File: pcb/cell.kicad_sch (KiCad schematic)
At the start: 29 parts, among them U1 MC74HC151ADTR2G, U2 SN74LVC1G74

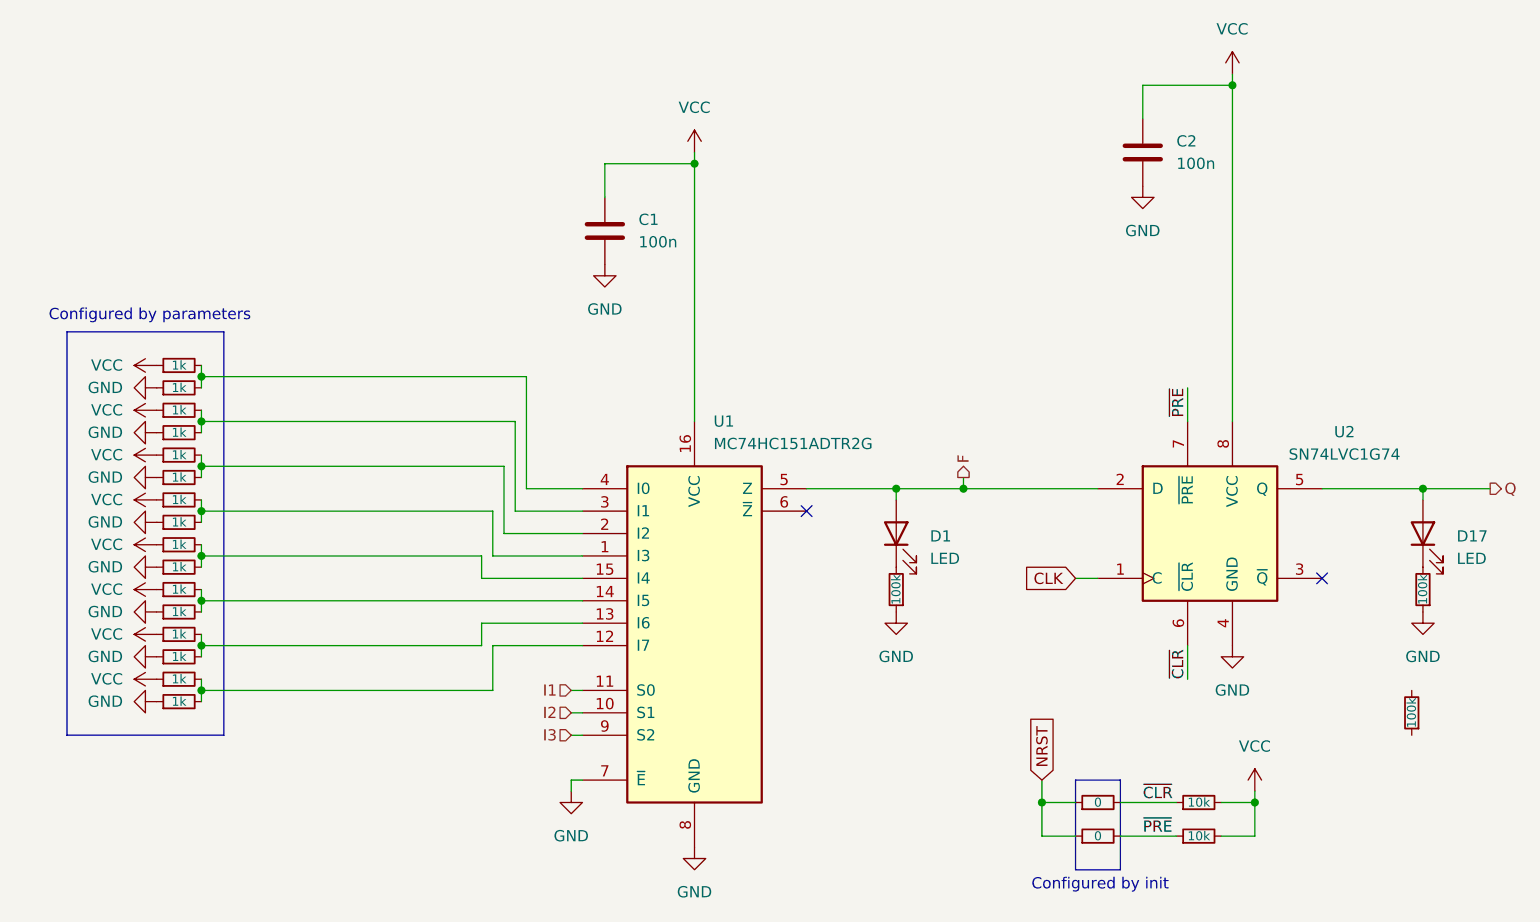
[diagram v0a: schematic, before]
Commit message: Add output LED array
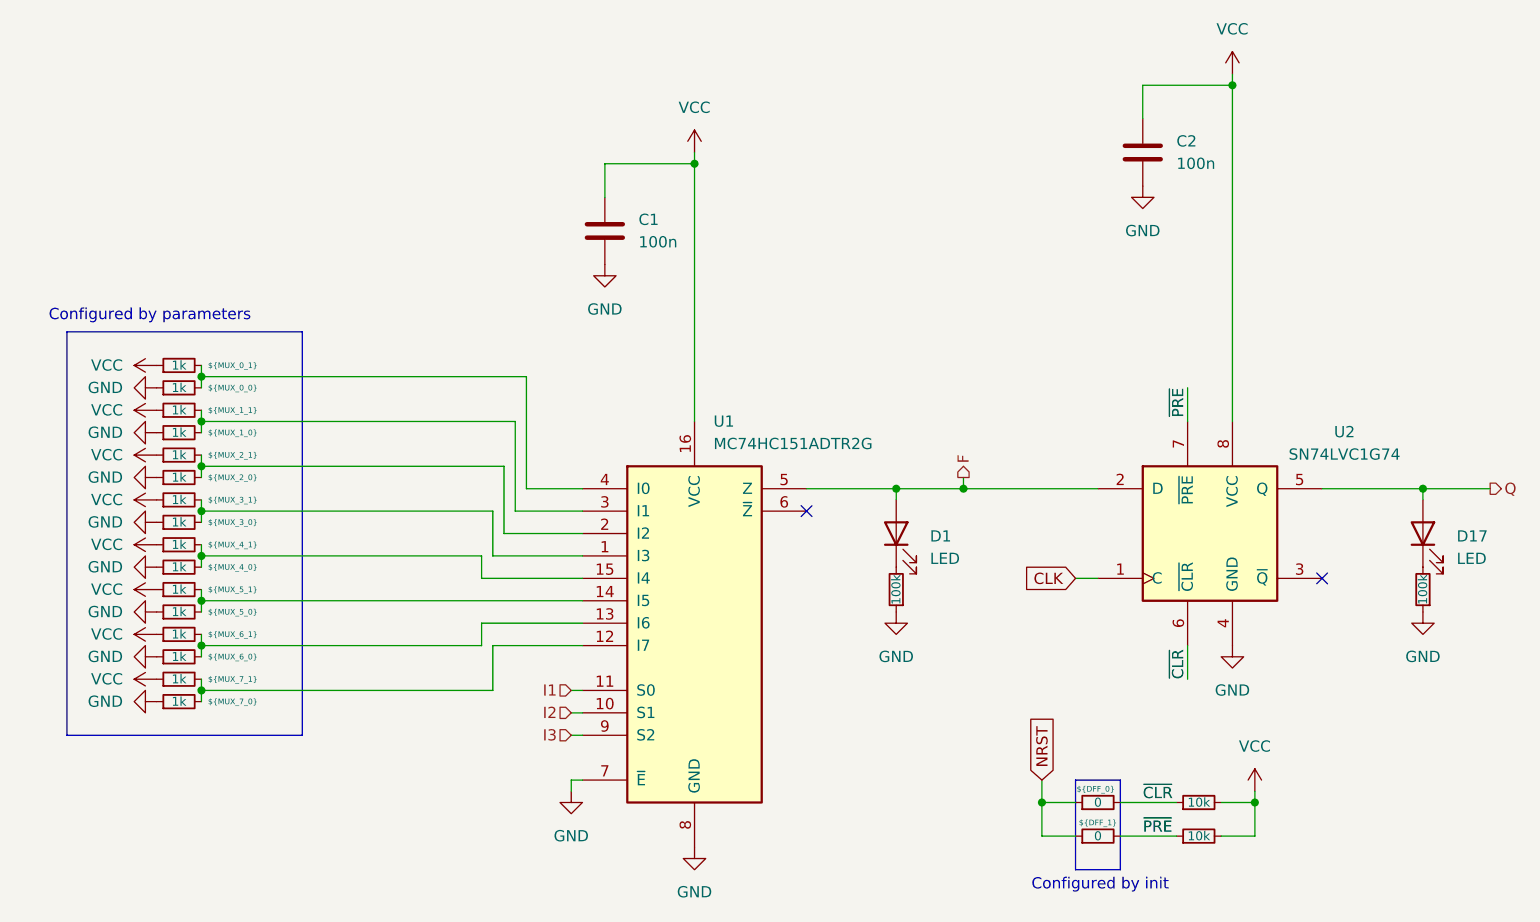
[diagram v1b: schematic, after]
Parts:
- removed R40: 100k, Resistor_SMD:R_0402_1005Metric, symbol Device:R_Small
- R1: POPULATE (none) -> ${MUX_0_0}
- R10: POPULATE (none) -> ${MUX_4_0}
- R11: POPULATE (none) -> ${MUX_5_1}
- R12: POPULATE (none) -> ${MUX_5_0}
- R13: POPULATE (none) -> ${MUX_6_1}
- R14: POPULATE (none) -> ${MUX_6_0}
- R15: POPULATE (none) -> ${MUX_7_1}
- R16: POPULATE (none) -> ${MUX_7_0}
- R2: POPULATE (none) -> ${MUX_1_1}
- R3: POPULATE (none) -> ${MUX_0_1}
- R35: POPULATE (none) -> ${DFF_0}
- R36: POPULATE (none) -> ${DFF_1}
- R4: POPULATE (none) -> ${MUX_1_0}
- R5: POPULATE (none) -> ${MUX_2_1}
- R6: ${MUX_2_0} (none) -> ${MUX_2_0}
- R7: POPULATE (none) -> ${MUX_3_1}
- R8: POPULATE (none) -> ${MUX_3_0}
- R9: POPULATE (none) -> ${MUX_4_1}
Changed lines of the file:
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@@
 	(rectangle
 		(start 68.58 58.42)
-		(end 86.36 104.14)
+		(end 95.25 104.14)
 		(stroke
 			(width 0)
@@
 			)
 		)
+		(property "POPULATE" "${MUX_0_1}"
+			(at 87.376 62.23 90)
+			(effects
+				(font
+					(size 0.635 0.635)
+				)
+			)
+		)
 		(pin "2"
 		)
@@
 			)
 		)
+		(property "POPULATE" "${MUX_4_0}"
+			(at 87.376 85.09 90)
+			(effects
+				(font
+					(size 0.635 0.635)
+				)
+			)
+		)
 		(pin "2"
 		)
@@
 			)
 		)
+		(property "POPULATE" "${MUX_5_1}"
+			(at 87.376 87.63 90)
+			(effects
+				(font
+					(size 0.635 0.635)
+				)
+			)
+		)
 		(pin "2"
 		)
@@
 			)
 		)
+		(property "POPULATE" "${MUX_2_1}"
+			(at 87.376 72.39 90)
+			(effects
+				(font
+					(size 0.635 0.635)
+				)
+			)
+		)
 		(pin "2"
 		)
@@
 			)
 		)
+		(property "POPULATE" "${DFF_1}"
+			(at 185.42 114.046 90)
+			(effects
+				(font
+					(size 0.635 0.635)
+				)
+			)
+		)
 		(pin "2"
 		)
@@
 			)
 		)
+		(property "POPULATE" "${MUX_1_0}"
+			(at 87.376 69.85 90)
+			(effects
+				(font
+					(size 0.635 0.635)
+				)
+			)
+		)
 		(pin "2"
 		)
@@
 			)
 		)
+		(property "POPULATE" "${DFF_0}"
+			(at 185.166 110.236 90)
+			(effects
+				(font
+					(size 0.635 0.635)
+				)
+			)
+		)
 		(pin "2"
 		)
@@
 			)
 		)
+		(property "POPULATE" "${MUX_7_1}"
+			(at 87.376 97.79 90)
+			(effects
+				(font
+					(size 0.635 0.635)
+				)
+			)
+		)
 		(pin "2"
 		)
@@
 			)
 		)
+		(property "POPULATE" "${MUX_4_1}"
+			(at 87.376 82.55 90)
+			(effects
+				(font
+					(size 0.635 0.635)
+				)
+			)
+		)
 		(pin "2"
 		)
@@
 			)
 		)
+		(property "POPULATE" "${MUX_3_1}"
+			(at 87.376 77.47 90)
+			(effects
+				(font
+					(size 0.635 0.635)
+				)
+			)
+		)
 		(pin "2"
 		)
@@
 			)
 		)
+		(property "POPULATE" "${MUX_3_0}"
+			(at 87.376 80.01 90)
+			(effects
+				(font
+					(size 0.635 0.635)
+				)
+			)
+		)
 		(pin "2"
 		)
@@
 			)
 		)
+		(property "POPULATE" "${MUX_1_1}"
+			(at 87.376 67.31 90)
+			(effects
+				(font
+					(size 0.635 0.635)
+				)
+			)
+		)
 		(pin "2"
 		)
@@
 			)
 		)
+		(property "POPULATE" "${MUX_0_0}"
+			(at 87.376 64.77 90)
+			(effects
+				(font
+					(size 0.635 0.635)
+				)
+			)
+		)
 		(pin "2"
 		)
@@
 			)
 		)
+		(property "POPULATE" "${MUX_6_1}"
+			(at 87.376 92.71 90)
+			(effects
+				(font
+					(size 0.635 0.635)
+				)
+			)
+		)
 		(pin "2"
 		)
@@
 			)
 		)
+		(property "${MUX_2_0}" "${MUX_2_0}"
+			(at 87.376 74.93 90)
+			(effects
+				(font
+					(size 0.635 0.635)
+				)
+			)
+		)
 		(pin "2"
 		)
@@
 			)
 		)
+		(property "POPULATE" "${MUX_7_0}"
+			(at 87.376 100.33 90)
+			(effects
+				(font
+					(size 0.635 0.635)
+				)
+			)
+		)
 		(pin "2"
 		)
@@
 			)
 		)
-		(pin "2"
-		)
-		(pin "1"
-		)
-		(instances
-			(project "74aoc"
-				(path "/976aec4d-1ebe-44c6-a45c-c82e0c896ea2/7fc5f80c-ae61-41ba-be16-2c640c59fc3f"
-					(reference "R12")
-					(unit 1)
-				)
-			)
-		)
-	)
-	(symbol
-		(lib_id "Device:R_Small")
-		(at 220.98 101.6 180)
-		(unit 1)
-		(exclude_from_sim no)
-		(in_bom yes)
-		(on_board yes)
-		(dnp no)
-		(property "Reference" "R40"
-			(at 222.25 98.806 90)
+		(property "POPULATE" "${MUX_5_0}"
+			(at 87.376 90.17 90)
 			(effects
 				(font
-					(size 1.016 1.016)
+					(size 0.635 0.635)
 				)
-				(hide yes)
-			)
-		)
-		(property "Value" "100k"
-			(at 220.98 101.6 90)
-			(effects
-				(font
-					(size 1.016 1.016)
-				)
-			)
-		)
-		(property "Footprint" "Resistor_SMD:R_0402_1005Metric"
-			(at 220.98 101.6 0)
-			(effects
-				(font
-					(size 1.27 1.27)
-				)
-				(hide yes)
-			)
-		)
-		(property "Datasheet" "~"
-			(at 220.98 101.6 0)
-			(effects
-				(font
-					(size 1.27 1.27)
-				)
-				(hide yes)
-			)
-		)
-		(property "Description" "Resistor, small symbol"
-			(at 220.98 101.6 0)
-			(effects
-				(font
-					(size 1.27 1.27)
-				)
-				(hide yes)
 			)
 		)
@@
 			(project "74aoc"
 				(path "/976aec4d-1ebe-44c6-a45c-c82e0c896ea2/7fc5f80c-ae61-41ba-be16-2c640c59fc3f"
-					(reference "R40")
+					(reference "R12")
 					(unit 1)
 				)
@@
 			)
 		)
+		(property "POPULATE" "${MUX_6_0}"
+			(at 87.376 95.25 90)
+			(effects
+				(font
+					(size 0.635 0.635)
+				)
+			)
+		)

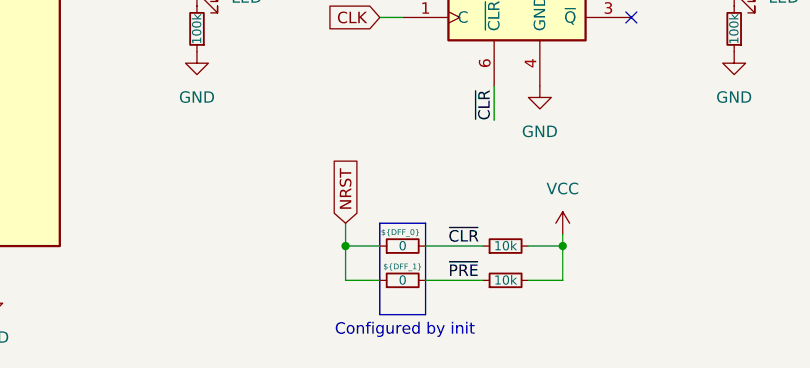
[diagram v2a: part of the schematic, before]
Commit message: Initialize all DFFs to 0
Oops did not realize that nextpnr can only do 1 anyway...
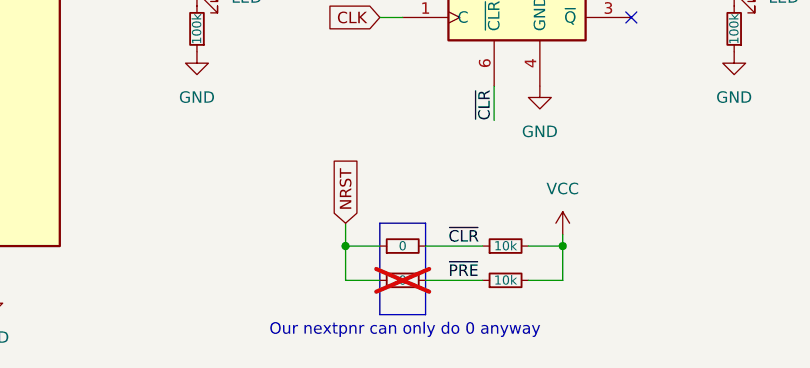
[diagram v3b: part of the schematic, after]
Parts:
- R35: POPULATE ${DFF_0} -> (none)
- R36: POPULATE ${DFF_1} -> (none); now not fitted
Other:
- note added: "Our nextpnr can only do 0 anyway"
- note removed: "Configured by init"
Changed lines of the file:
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@@
 		)
 	)
-	(text "Configured by init"
+	(text "Our nextpnr can only do 0 anyway"
 		(exclude_from_sim no)
 		(at 185.674 121.158 0)
@@
 		(in_bom yes)
 		(on_board yes)
-		(dnp no)
+		(dnp yes)
 		(property "Reference" "R36"
 			(at 188.214 116.84 90)
@@
 			)
 		)
-		(property "POPULATE" "${DFF_1}"
-			(at 185.42 114.046 90)
-			(effects
-				(font
-					(size 0.635 0.635)
-				)
-			)
-		)
 		(pin "2"
 		)
@@
 			)
 		)
-		(property "POPULATE" "${DFF_0}"
-			(at 185.166 110.236 90)
-			(effects
-				(font
-					(size 0.635 0.635)
-				)
-			)
-		)

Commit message: PCB prettification
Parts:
- U2: POPULATE (none) -> ${USE_DFF}
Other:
- note added: "Nextpnr can only do 0 anyway"
- note removed: "Our nextpnr can only do 0 anyway"
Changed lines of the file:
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@@
 		)
 	)
-	(text "Our nextpnr can only do 0 anyway"
+	(text "Nextpnr can only do 0 anyway"
 		(exclude_from_sim no)
 		(at 185.674 121.158 0)
@@
 			(at 198.12 81.28 0)
 			(effects
+				(font
+					(size 1.27 1.27)
+				)
+				(hide yes)
+			)
+		)
+		(property "POPULATE" "${USE_DFF}"
+			(at 198.12 81.28 0)
+			(effects

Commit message: Tag unused Muxes/DFFs for not-populating
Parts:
- U1: POPULATE (none) -> ${USE_MUX}
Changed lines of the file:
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@@
+			)
+		)
+		(property "POPULATE" "${USE_MUX}"
+			(at 139.7 91.44 0)
+			(effects
+				(font
+					(size 1.27 1.27)
+				)
+				(hide yes)
 			)
 		)

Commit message: Add LCSC codes to everything that did not have them yet
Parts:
- C1, C2: LCSC (none) -> C1525
- R1, R10, R11, R12, R13, R14, R15, R16, R2, R3, R4, R5, R6, R7, R8, R9: LCSC (none) -> C11702
- R17, R34: LCSC (none) -> C25744
- R35, R36: LCSC (none) -> C17168
- R37, R38: LCSC (none) -> C25741
- U1: LCSC (none) -> C152523
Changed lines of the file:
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@@
 			)
 		)
+		(property "LCSC" "C11702"
+			(at 81.28 62.23 90)
+			(effects
+				(font
+					(size 1.27 1.27)
+				)
+				(hide yes)
+			)
+		)
 		(pin "2"
 		)
@@
 			)
 		)
+		(property "LCSC" "C11702"
+			(at 81.28 85.09 90)
+			(effects
+				(font
+					(size 1.27 1.27)
+				)
+				(hide yes)
+			)
+		)
 		(pin "2"
 		)
@@
 			)
 		)
+		(property "LCSC" "C11702"
+			(at 81.28 87.63 90)
+			(effects
+				(font
+					(size 1.27 1.27)
+				)
+				(hide yes)
+			)
+		)
 		(pin "2"
 		)
@@
 			)
 		)
+		(property "LCSC" "C25744"
+			(at 196.85 115.57 90)
+			(effects
+				(font
+					(size 1.27 1.27)
+				)
+				(hide yes)
+			)
+		)
 		(pin "2"
 		)
@@
 			)
 		)
+		(property "LCSC" "C11702"
+			(at 81.28 72.39 90)
+			(effects
+				(font
+					(size 1.27 1.27)
+				)
+				(hide yes)
+			)
+		)
 		(pin "2"
 		)
@@
 			)
 		)
+		(property "LCSC" "C17168"
+			(at 185.42 115.57 90)
+			(effects
+				(font
+					(size 1.27 1.27)
+				)
+				(hide yes)
+			)
+		)
 		(pin "2"
 		)
@@
 			)
 		)
+		(property "LCSC" "C11702"
+			(at 81.28 69.85 90)
+			(effects
+				(font
+					(size 1.27 1.27)
+				)
+				(hide yes)
+			)
+		)
 		(pin "2"
 		)
@@
 			)
 		)
+		(property "LCSC" "C17168"
+			(at 185.42 111.76 90)
+			(effects
+				(font
+					(size 1.27 1.27)
+				)
+				(hide yes)
+			)
+		)
 		(pin "2"
 		)
@@
 			)
 		)
+		(property "LCSC" "C11702"
+			(at 81.28 97.79 90)
+			(effects
+				(font
+					(size 1.27 1.27)
+				)
+				(hide yes)
+			)
+		)
 		(pin "2"
 		)
@@
 			)
 		)
+		(property "LCSC" "C25741"
+			(at 162.56 87.63 90)
+			(effects
+				(font
+					(size 1.27 1.27)
+				)
+				(hide yes)
+			)
+		)
 		(pin "2"
 		)
@@
 			)
 		)
+		(property "LCSC" "C11702"
+			(at 81.28 82.55 90)
+			(effects
+				(font
+					(size 1.27 1.27)
+				)
+				(hide yes)
+			)
+		)
 		(pin "2"
 		)
@@
 			)
 		)
+		(property "LCSC" "C25744"
+			(at 196.85 111.76 90)
+			(effects
+				(font
+					(size 1.27 1.27)
+				)
+				(hide yes)
+			)
+		)
 		(pin "2"
 		)
@@
 			)
 		)
+		(property "LCSC" "C11702"
+			(at 81.28 77.47 90)
+			(effects
+				(font
+					(size 1.27 1.27)
+				)
+				(hide yes)
+			)
+		)
 		(pin "2"
 		)
@@
 			)
 		)
+		(property "LCSC" "C11702"
+			(at 81.28 80.01 90)
+			(effects
+				(font
+					(size 1.27 1.27)
+				)
+				(hide yes)
+			)
+		)
 		(pin "2"
 		)
@@
 			)
 		)
+		(property "LCSC" "C1525"
+			(at 129.54 46.99 0)
+			(effects
+				(font
+					(size 1.27 1.27)
+				)
+				(hide yes)
+			)
+		)
 		(pin "1"
 		)
@@
 			)
 		)
+		(property "LCSC" "C11702"
+			(at 81.28 67.31 90)
+			(effects
+				(font
+					(size 1.27 1.27)
+				)
+				(hide yes)
+			)
+		)
 		(pin "2"
 		)
@@
 			)
 		)
+		(property "LCSC" "C11702"
+			(at 81.28 64.77 90)
+			(effects
+				(font
+					(size 1.27 1.27)
+				)
+				(hide yes)
+			)
+		)
 		(pin "2"
 		)
@@
 			)
 		)
+		(property "LCSC" "C1525"
+			(at 190.5 38.1 0)
+			(effects
+				(font
+					(size 1.27 1.27)
+				)
+				(hide yes)
+			)
+		)
 		(pin "1"
 		)
@@
 			)
 		)
+		(property "LCSC" "C25741"
+			(at 222.25 87.63 90)
+			(effects
+				(font
+					(size 1.27 1.27)
+				)
+				(hide yes)
+			)
+		)
 		(pin "2"
 		)
@@
 			)
 		)
+		(property "LCSC" "C11702"
+			(at 81.28 92.71 90)
+			(effects
+				(font
+					(size 1.27 1.27)
+				)
+				(hide yes)
+			)
+		)
 		(pin "2"
 		)
@@
 			)
 		)
+		(property "LCSC" "C11702"
+			(at 81.28 74.93 90)
+			(effects
+				(font
+					(size 1.27 1.27)
+				)
+				(hide yes)
+			)
+		)
 		(pin "2"
 		)
@@
 			)
 		)
+		(property "LCSC" "C11702"
+			(at 81.28 100.33 90)
+			(effects
+				(font
+					(size 1.27 1.27)
+				)
+				(hide yes)
+			)
+		)
 		(pin "2"
 		)
@@
 			)
 		)
+		(property "LCSC" "C11702"
+			(at 81.28 90.17 90)
+			(effects
+				(font
+					(size 1.27 1.27)
+				)
+				(hide yes)
+			)
+		)
 		(pin "2"
 		)
@@
 			)
 		)
+		(property "LCSC" "C11702"
+			(at 81.28 95.25 90)
+			(effects
+				(font
+					(size 1.27 1.27)
+				)
+				(hide yes)
+			)
+		)
 		(pin "2"
 		)
@@
 			(at 139.7 91.44 0)
 			(effects
+				(font
+					(size 1.27 1.27)
+				)
+				(hide yes)
+			)
+		)
+		(property "LCSC" "C152523"
+			(at 139.7 91.44 0)
+			(effects

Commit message: Add JLCPCB_CORRECTION
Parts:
- U1: JLCPCB_CORRECTION (none) -> 0;0;270
- U2: JLCPCB_CORRECTION (none) -> 0;0;180
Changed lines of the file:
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@@
 			)
 		)
+		(property "JLCPCB_CORRECTION" "0;0;180"
+			(at 198.12 81.28 0)
+			(effects
+				(font
+					(size 1.27 1.27)
+				)
+				(hide yes)
+			)
+		)
 		(pin "8"
 		)
@@
 			(at 139.7 91.44 0)
 			(effects
+				(font
+					(size 1.27 1.27)
+				)
+				(hide yes)
+			)
+		)
+		(property "JLCPCB_CORRECTION" "0;0;270"
+			(at 139.7 91.44 0)
+			(effects
